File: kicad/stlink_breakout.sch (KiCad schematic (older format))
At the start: 2 parts, among them P1 CONN_01X06, P2 CONN_02X10

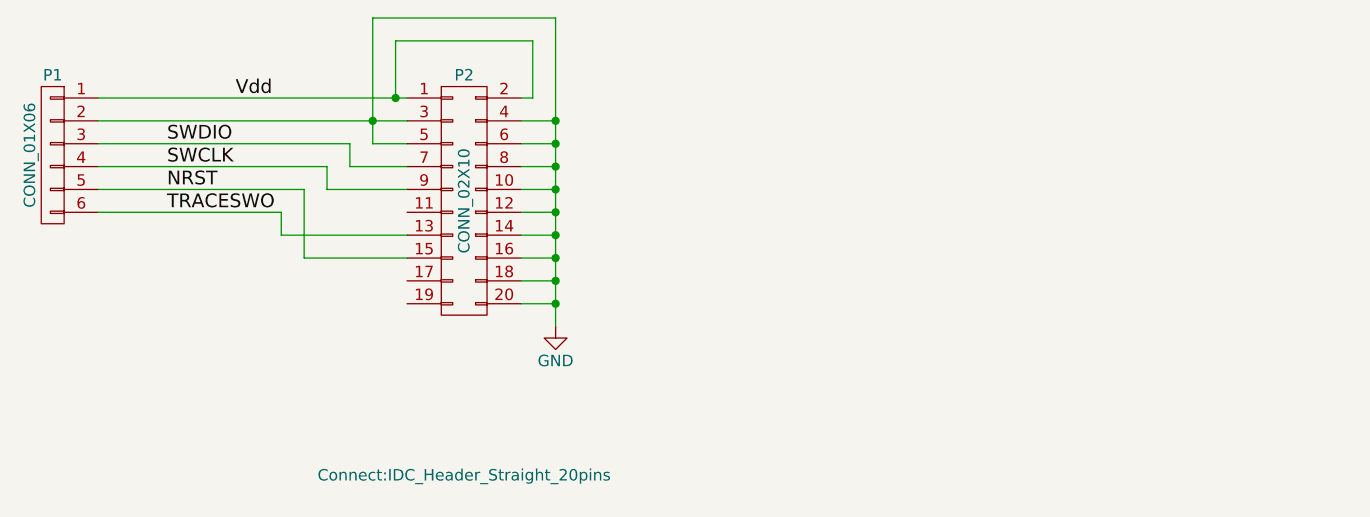
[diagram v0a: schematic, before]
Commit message: Added schematic page info
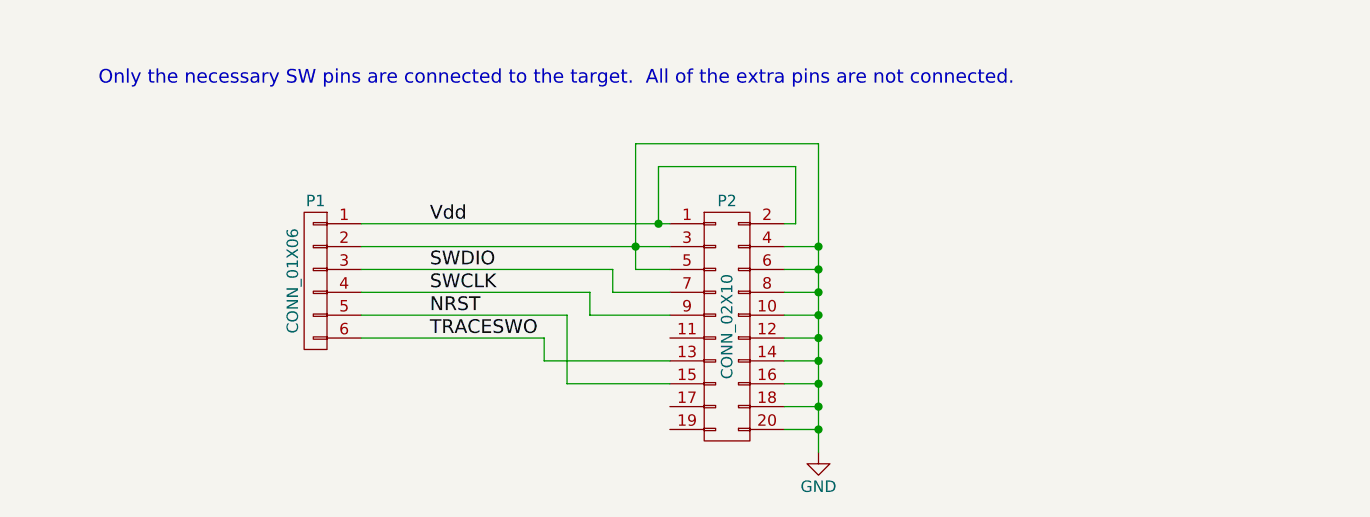
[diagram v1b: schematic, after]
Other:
- note added: "Only the necessary SW pins are connected to the target. All of the extra pins are not connected."
- moved on the sheet: P1, P2
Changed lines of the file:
@@
 LIBS:contrib
 LIBS:valves
+LIBS:stlink_breakout-cache
 EELAYER 25 0
 EELAYER END
@@
 encoding utf-8
 Sheet 1 1
-Title ""
-Date ""
-Rev ""
-Comp ""
+Title "STLINK/V2 Breakout"
+Date "2016-06-16"
+Rev "0.1"
+Comp "for(embed)"
 Comment1 ""
 Comment2 ""
@@
 L CONN_02X10 P2
 U 1 1 5763B28B
-P 4900 3200
-F 0 "P2" H 4900 3750 50  0000 C CNN
-F 1 "CONN_02X10" V 4900 3200 50  0000 C CNN
-F 2 "Connect:IDC_Header_Straight_20pins" H 4900 2000 50  0000 C CNN
-F 3 "" H 4900 2000 50  0000 C CNN
-	1    4900 3200
+P 6050 3750
+F 0 "P2" H 6050 4300 50  0000 C CNN
+F 1 "CONN_02X10" V 6050 3750 50  0000 C CNN
+F 2 "Connect:IDC_Header_Straight_20pins" H 6050 2550 50  0001 C CNN
+F 3 "" H 6050 2550 50  0000 C CNN
+	1    6050 3750
 	1    0    0    -1
 $EndComp
@@
 L GND #PWR1
 U 1 1 5763B341
-P 5300 3750
-F 0 "#PWR1" H 5300 3500 50  0001 C CNN
-F 1 "GND" H 5300 3600 50  0000 C CNN
-F 2 "" H 5300 3750 50  0000 C CNN
-F 3 "" H 5300 3750 50  0000 C CNN
-	1    5300 3750
+P 6450 4300
+F 0 "#PWR1" H 6450 4050 50  0001 C CNN
+F 1 "GND" H 6450 4150 50  0000 C CNN
+F 2 "" H 6450 4300 50  0000 C CNN
+F 3 "" H 6450 4300 50  0000 C CNN
+	1    6450 4300
 	1    0    0    -1
 $EndComp
 Wire Wire Line
-	5300 2400 5300 3750
+	6450 2950 6450 4300
 Wire Wire Line
-	5300 2850 5150 2850
+	6450 3400 6300 3400
 Wire Wire Line
-	3300 2850 4650 2850
+	4450 3400 5800 3400
 Wire Wire Line
-	5150 2950 5300 2950
-Connection ~ 5300 2950
+	6300 3500 6450 3500
+Connection ~ 6450 3500
 Wire Wire Line
-	5150 3050 5300 3050
-Connection ~ 5300 3050
+	6300 3600 6450 3600
+Connection ~ 6450 3600
 Wire Wire Line
-	5150 3150 5300 3150
-Connection ~ 5300 3150
+	6300 3700 6450 3700
+Connection ~ 6450 3700
 Wire Wire Line
-	5150 3250 5300 3250
-Connection ~ 5300 3250
+	6300 3800 6450 3800
+Connection ~ 6450 3800
 Wire Wire Line
-	5150 3350 5300 3350
-Connection ~ 5300 3350
+	6300 3900 6450 3900
+Connection ~ 6450 3900
 Wire Wire Line
-	5150 3450 5300 3450
-Connection ~ 5300 3450
+	6300 4000 6450 4000
+Connection ~ 6450 4000
 Wire Wire Line
-	5150 3550 5300 3550
-Connection ~ 5300 3550
+	6300 4100 6450 4100
+Connection ~ 6450 4100
 Wire Wire Line
-	5150 3650 5300 3650
-Connection ~ 5300 3650
+	6300 4200 6450 4200
+Connection ~ 6450 4200
 $Comp
 L CONN_01X06 P1
 U 1 1 5763B464
-P 3100 3000
-F 0 "P1" H 3100 3350 50  0000 C CNN
-F 1 "CONN_01X06" V 3200 3000 50  0000 C CNN
-F 2 "kicad_pcb:CON_1x6_0.1in" H 3100 3000 50  0001 C CNN
-F 3 "" H 3100 3000 50  0000 C CNN
-	1    3100 3000
+P 4250 3550
+F 0 "P1" H 4250 3900 50  0000 C CNN
+F 1 "CONN_01X06" V 4350 3550 50  0000 C CNN
+F 2 "kicad_pcb:CON_1x6_0.1in" H 4250 3550 50  0001 C CNN
+F 3 "" H 4250 3550 50  0000 C CNN
+	1    4250 3550
 	-1   0    0    -1
 $EndComp
 Wire Wire Line
-	3300 2750 4650 2750
-Connection ~ 4500 2850
+	4450 3300 5800 3300
+Connection ~ 5650 3400
 Wire Wire Line
-	4500 2950 4650 2950
+	5650 3500 5800 3500
 Wire Wire Line
-	4500 2400 4500 2950
+	5650 2950 5650 3500
 Wire Wire Line
-	4500 2400 5300 2400
-Connection ~ 5300 2850
+	5650 2950 6450 2950
+Connection ~ 6450 3400
 Wire Wire Line
-	5150 2750 5200 2750
+	6300 3300 6350 3300
 Wire Wire Line
-	5200 2750 5200 2500
+	6350 3300 6350 3050
 Wire Wire Line
-	5200 2500 4600 2500
+	6350 3050 5750 3050
 Wire Wire Line
-	4600 2500 4600 2750
-Connection ~ 4600 2750
-Text Label 3900 2750 0    60   ~ 0
+	5750 3050 5750 3300
+Connection ~ 5750 3300
+Text Label 4750 3300 0    60   ~ 0
 Vdd
 Wire Wire Line
-	3300 2950 4400 2950
+	4450 3500 5550 3500
 Wire Wire Line
-	4400 2950 4400 3050
+	5550 3500 5550 3600
 Wire Wire Line
-	4400 3050 4650 3050
+	5550 3600 5800 3600
 Wire Wire Line
-	3300 3050 4300 3050
+	4450 3600 5450 3600
 Wire Wire Line
-	4300 3050 4300 3150
+	5450 3600 5450 3700
 Wire Wire Line
-	4300 3150 4650 3150
-Text Label 3600 2950 0    60   ~ 0
+	5450 3700 5800 3700
+Text Label 4750 3500 0    60   ~ 0
 SWDIO
-Text Label 3600 3050 0    60   ~ 0
+Text Label 4750 3600 0    60   ~ 0
 SWCLK
 Wire Wire Line
-	4650 3450 4200 3450
+	5800 4000 5350 4000
 Wire Wire Line
-	4200 3450 4200 3150
+	5350 4000 5350 3700
 Wire Wire Line
-	4200 3150 3300 3150
-Text Label 3600 3150 0    60   ~ 0
+	5350 3700 4450 3700
+Text Label 4750 3700 0    60   ~ 0
 NRST
 Wire Wire Line
-	3300 3250 4100 3250
+	4450 3800 5250 3800
 Wire Wire Line
-	4100 3250 4100 3350
+	5250 3800 5250 3900
 Wire Wire Line
-	4100 3350 4650 3350
-Text Label 3600 3250 0    60   ~ 0
+	5250 3900 5800 3900
+Text Label 4750 3800 0    60   ~ 0
 TRACESWO
+Text Notes 3300 2700 0    60   ~ 0
+Only the necessary SW pins are connected to the target.  All of the extra pins are not connected.
 $EndSCHEMATC
